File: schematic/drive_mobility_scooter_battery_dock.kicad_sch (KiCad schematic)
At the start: 6 parts, among them J1 0V, J2 +25V, J3 25V, J4 0V

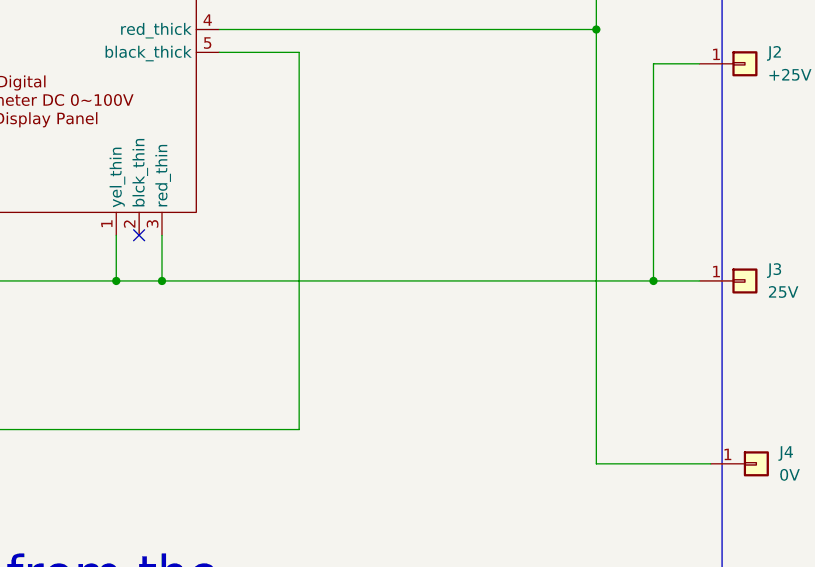
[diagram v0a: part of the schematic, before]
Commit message: - Add fuse. - Update documentation.
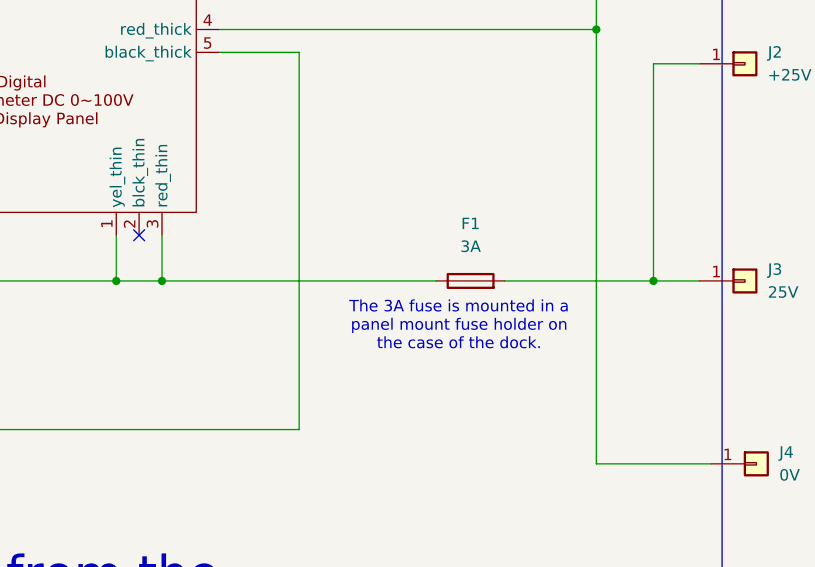
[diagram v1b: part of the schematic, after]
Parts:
- added F1: 3A, symbol Device:Fuse
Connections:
- net at M1.1 (yel_thin), M1.3 (red_thin), XLR1.2: now also F1.1; no longer J2.1 (Pin_1), J3.1 (Pin_1)
- new net: F1.2, J2.1 (Pin_1), J3.1 (Pin_1)
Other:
- note added: "The 3A fuse is mounted in a panel mount fuse holder on the case of the dock."
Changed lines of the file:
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@@
 	(paper "A4")
+	(junction
+		(at 205.74 87.63)
+		(diameter 0)
+		(color 0 0 0 0)
+	)
 	(junction
 		(at 151.13 87.63)
@@
 		(color 0 0 0 0)
 	)
-	(junction
-		(at 205.74 87.63)
-		(diameter 0)
-		(color 0 0 0 0)
-	)
 	(no_connect
 		(at 148.59 82.55)
@@
 	(wire
 		(pts
-			(xy 151.13 87.63) (xy 205.74 87.63)
-		)
-		(stroke
-			(width 0)
-			(type default)
-		)
-	)
-	(wire
-		(pts
 			(xy 199.39 107.95) (xy 212.09 107.95)
 		)
@@
 	(wire
 		(pts
+			(xy 189.23 87.63) (xy 205.74 87.63)
+		)
+		(stroke
+			(width 0)
+			(type default)
+		)
+	)
+	(wire
+		(pts
 			(xy 146.05 87.63) (xy 151.13 87.63)
 		)
@@
 		(pts
 			(xy 205.74 87.63) (xy 205.74 63.5)
+		)
+		(stroke
+			(width 0)
+			(type default)
+		)
+	)
+	(wire
+		(pts
+			(xy 151.13 87.63) (xy 181.61 87.63)
 		)
 		(stroke
@@
 		(exclude_from_sim no)
 		(at 240.284 75.946 0)
+		(effects
+			(font
+				(size 1.27 1.27)
+			)
+		)
+	)
+	(text "The 3A fuse is mounted in a\npanel mount fuse holder on \nthe case of the dock."
+		(exclude_from_sim no)
+		(at 184.15 92.71 0)
 		(effects
 			(font
@@
 					(unit 1)
 				)
+			)
+		)
+	)
+	(symbol
+		(lib_id "Device:Fuse")
+		(at 185.42 87.63 90)
+		(unit 1)
+		(exclude_from_sim no)
+		(in_bom yes)
+		(on_board yes)
+		(dnp no)
+		(fields_autoplaced yes)
+		(property "Reference" "F1"
+			(at 185.42 81.28 90)
+			(effects
+				(font
+					(size 1.27 1.27)
+				)
+			)
+		)
+		(property "Value" "3A"
+			(at 185.42 83.82 90)
+			(effects
+				(font
+					(size 1.27 1.27)
+				)
+			)
+		)
+		(property "Footprint" ""
+			(at 185.42 89.408 90)
+			(effects
+				(font
+					(size 1.27 1.27)
+				)
+				(hide yes)
+			)
+		)
+		(property "Datasheet" "~"
+			(at 185.42 87.63 0)
+			(effects
+				(font
+					(size 1.27 1.27)
+				)
+				(hide yes)
+			)
+		)
+		(property "Description" "Fuse"
+			(at 185.42 87.63 0)
+			(effects
+				(font
+					(size 1.27 1.27)
+				)
+				(hide yes)
+			)
+		)
+		(pin "2"
+		)
+		(pin "1"
+		)
+		(instances
+			(project ""
+				(path "/b0f3f214-a008-4b65-bd75-e72926a96c4e"
+					(reference "F1")
+					(unit 1)
+				)

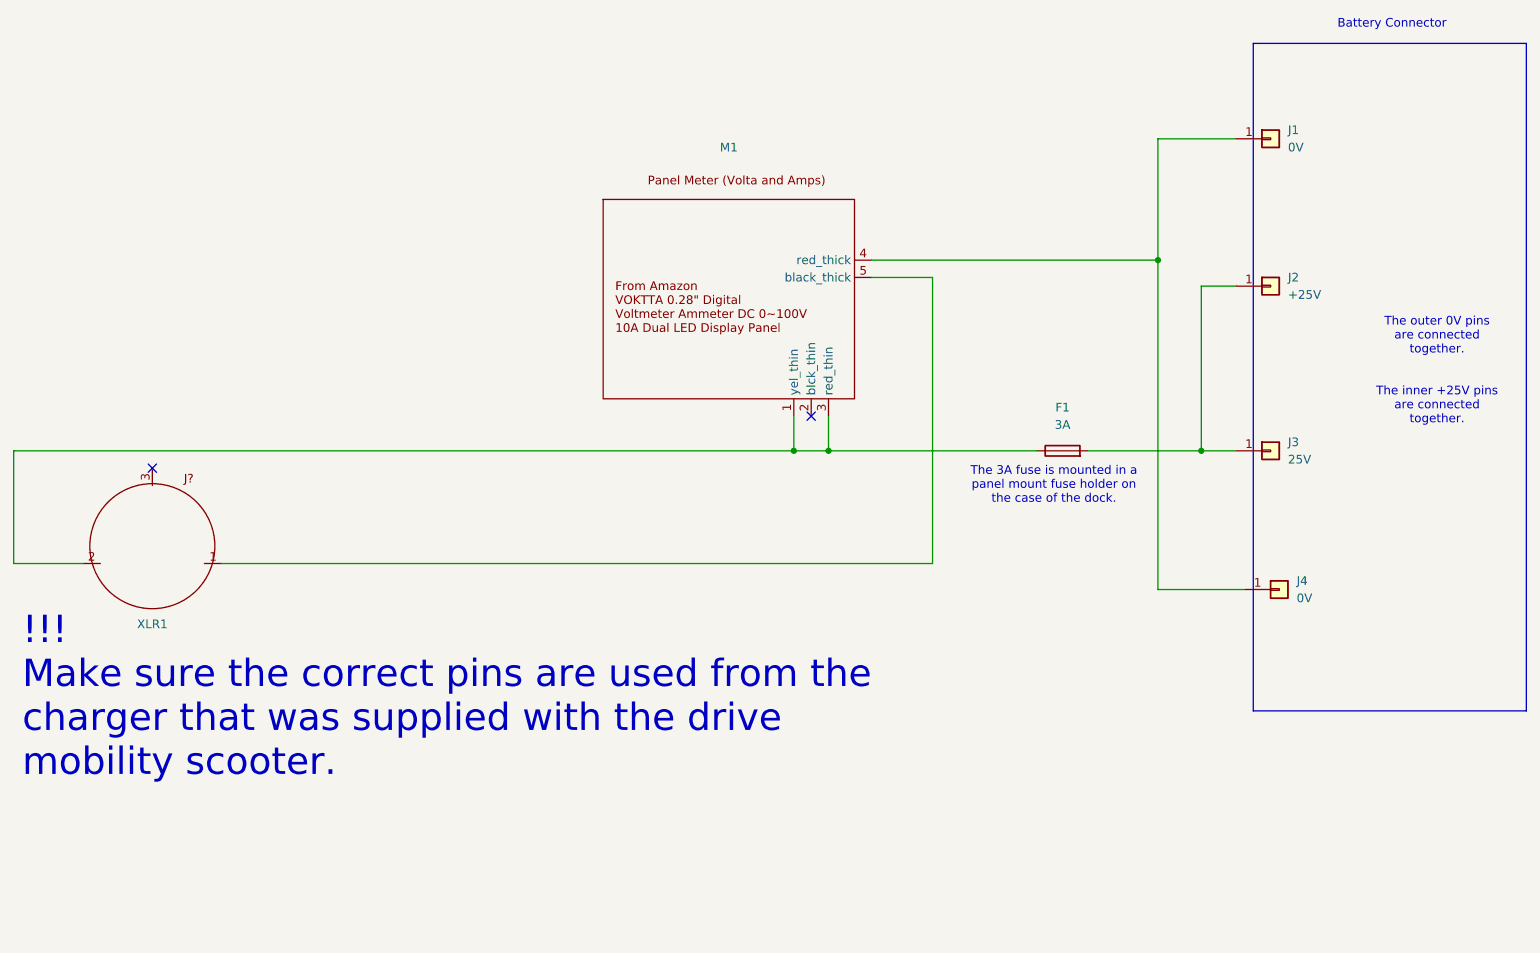
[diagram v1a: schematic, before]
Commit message: Add TVS device.
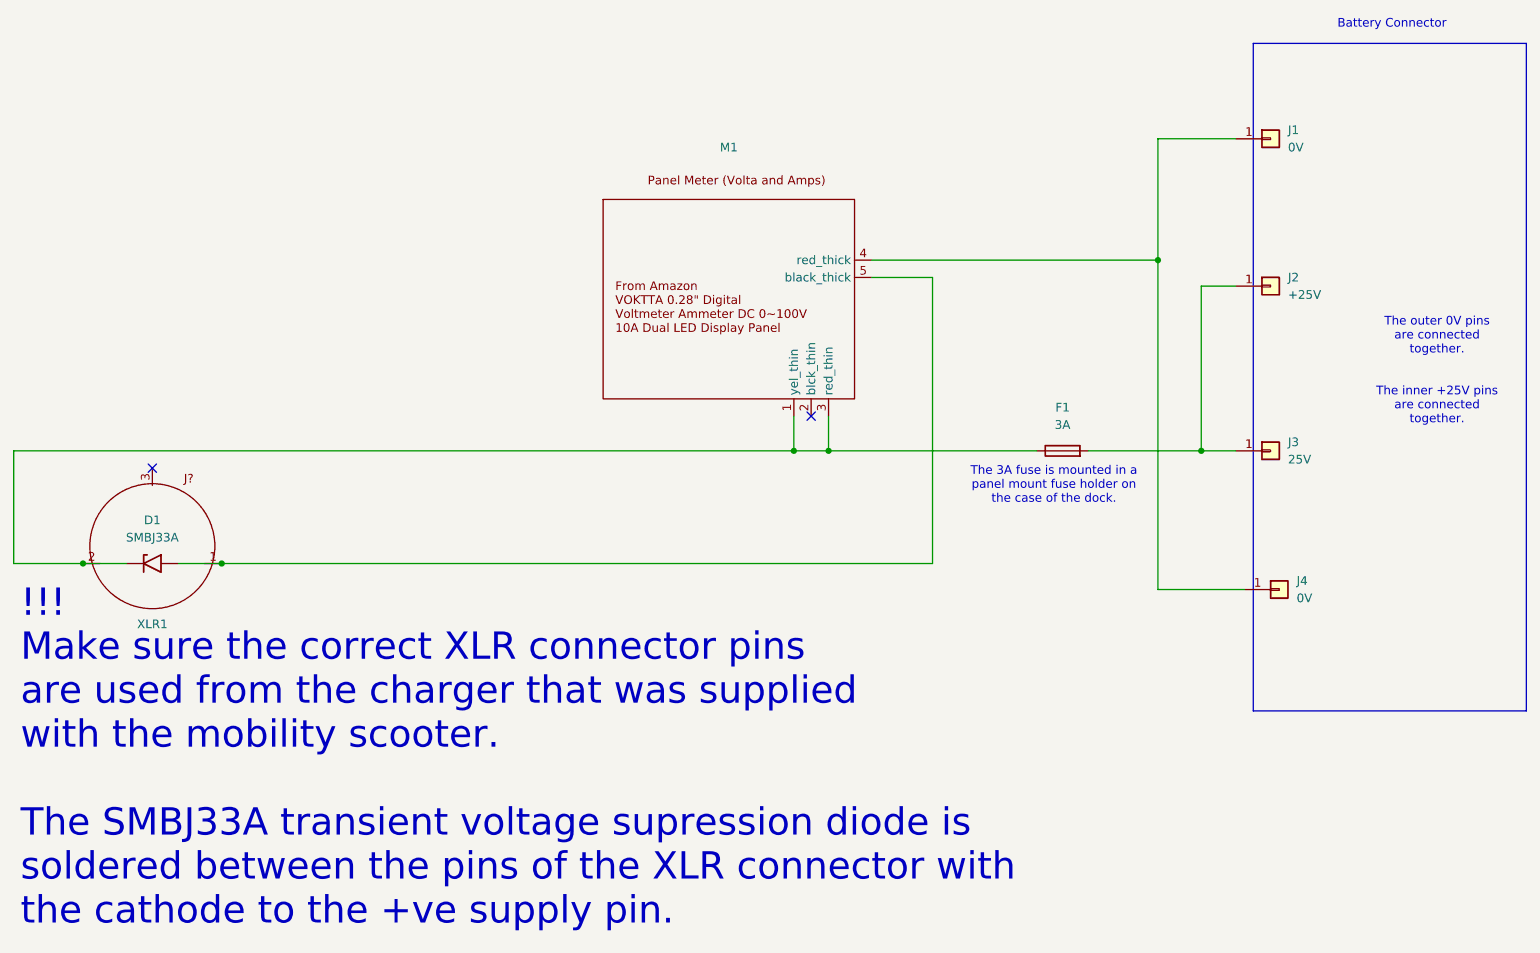
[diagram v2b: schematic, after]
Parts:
- added D1: SMBJ33A, Diode_SMD:D_SMA, symbol Diode:SMAJ60A
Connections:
- net at F1.1, M1.1 (yel_thin), M1.3 (red_thin)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: now also D1.1 (A1)
- net at M1.5 (black_thick), XLR1.1: now also D1.2 (A2)
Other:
- note added: "!!! Make sure the correct XLR connector pins are used from the charger that was supplied with the mobility scooter. The SMBJ33A transient voltage supression diode is soldered between the pins of the XLR connector with the cathode to the +ve supply pin."
- note removed: "!!! Make sure the correct pins are used from the charger that was supplied with the drive mobility scooter."
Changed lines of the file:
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@@
+	)
+	(junction
+		(at 62.23 104.14)
+		(diameter 0)
+		(color 0 0 0 0)
+	)
+	(junction
+		(at 41.91 104.14)
+		(diameter 0)
+		(color 0 0 0 0)
 	)
 	(junction
@@
 	(wire
 		(pts
-			(xy 41.91 104.14) (xy 31.75 104.14)
+			(xy 31.75 104.14) (xy 41.91 104.14)
 		)
 		(stroke
@@
 	(wire
 		(pts
+			(xy 55.88 104.14) (xy 62.23 104.14)
+		)
+		(stroke
+			(width 0)
+			(type default)
+		)
+	)
+	(wire
+		(pts
 			(xy 31.75 104.14) (xy 31.75 87.63)
 		)
@@
 		(pts
 			(xy 146.05 87.63) (xy 151.13 87.63)
+		)
+		(stroke
+			(width 0)
+			(type default)
+		)
+	)
+	(wire
+		(pts
+			(xy 41.91 104.14) (xy 48.26 104.14)
 		)
 		(stroke
@@
 		)
 	)
-	(text "!!! \nMake sure the correct pins are used from the \ncharger that was supplied with the drive \nmobility scooter."
-		(exclude_from_sim no)
-		(at 33.02 123.698 0)
+	(text "!!! \nMake sure the correct XLR connector pins \nare used from the charger that was supplied \nwith the mobility scooter.\n\nThe SMBJ33A transient voltage supression diode is\nsoldered between the pins of the XLR connector with\nthe cathode to the +ve supply pin."
+		(exclude_from_sim no)
+		(at 32.766 132.588 0)
 		(effects
 			(font
@@
 					(unit 1)
 				)
+			)
+		)
+	)
+	(symbol
+		(lib_id "Diode:SMAJ60A")
+		(at 52.07 104.14 0)
+		(unit 1)
+		(exclude_from_sim no)
+		(in_bom yes)
+		(on_board yes)
+		(dnp no)
+		(fields_autoplaced yes)
+		(property "Reference" "D1"
+			(at 52.07 97.79 0)
+			(effects
+				(font
+					(size 1.27 1.27)
+				)
+			)
+		)
+		(property "Value" "SMBJ33A"
+			(at 52.07 100.33 0)
+			(effects
+				(font
+					(size 1.27 1.27)
+				)
+			)
+		)
+		(property "Footprint" "Diode_SMD:D_SMA"
+			(at 52.07 109.22 0)
+			(effects
+				(font
+					(size 1.27 1.27)
+				)
+				(hide yes)
+			)
+		)
+		(property "Datasheet" "https://www.littelfuse.com/media?resourcetype=datasheets&itemid=75e32973-b177-4ee3-a0ff-cedaf1abdb93&filename=smaj-datasheet"
+			(at 50.8 104.14 0)
+			(effects
+				(font
+					(size 1.27 1.27)
+				)
+				(hide yes)
+			)
+		)
+		(property "Description" "400W unidirectional Transient Voltage Suppressor, 60.0Vr, SMA(DO-214AC)"
+			(at 52.07 104.14 0)
+			(effects
+				(font
+					(size 1.27 1.27)
+				)
+				(hide yes)
+			)
+		)
+		(pin "1"
+		)
+		(pin "2"
+		)
+		(instances
+			(project ""
+				(path "/b0f3f214-a008-4b65-bd75-e72926a96c4e"
+					(reference "D1")
+					(unit 1)
+				)
